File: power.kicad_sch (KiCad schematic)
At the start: 73 parts, among them J1 436500204, J2 ${MANUFACTURER PART NUMBER}, J3 ${MANUFACTURER PART NUMBER}, J4 398800302, J5 398800302, J6 398800302, J7 398800302, U2 INA229AQDGSRQ1, U3 ${MANUFACTURER PART NUMBER}, U4 ${MANUFACTURER PART NUMBER}

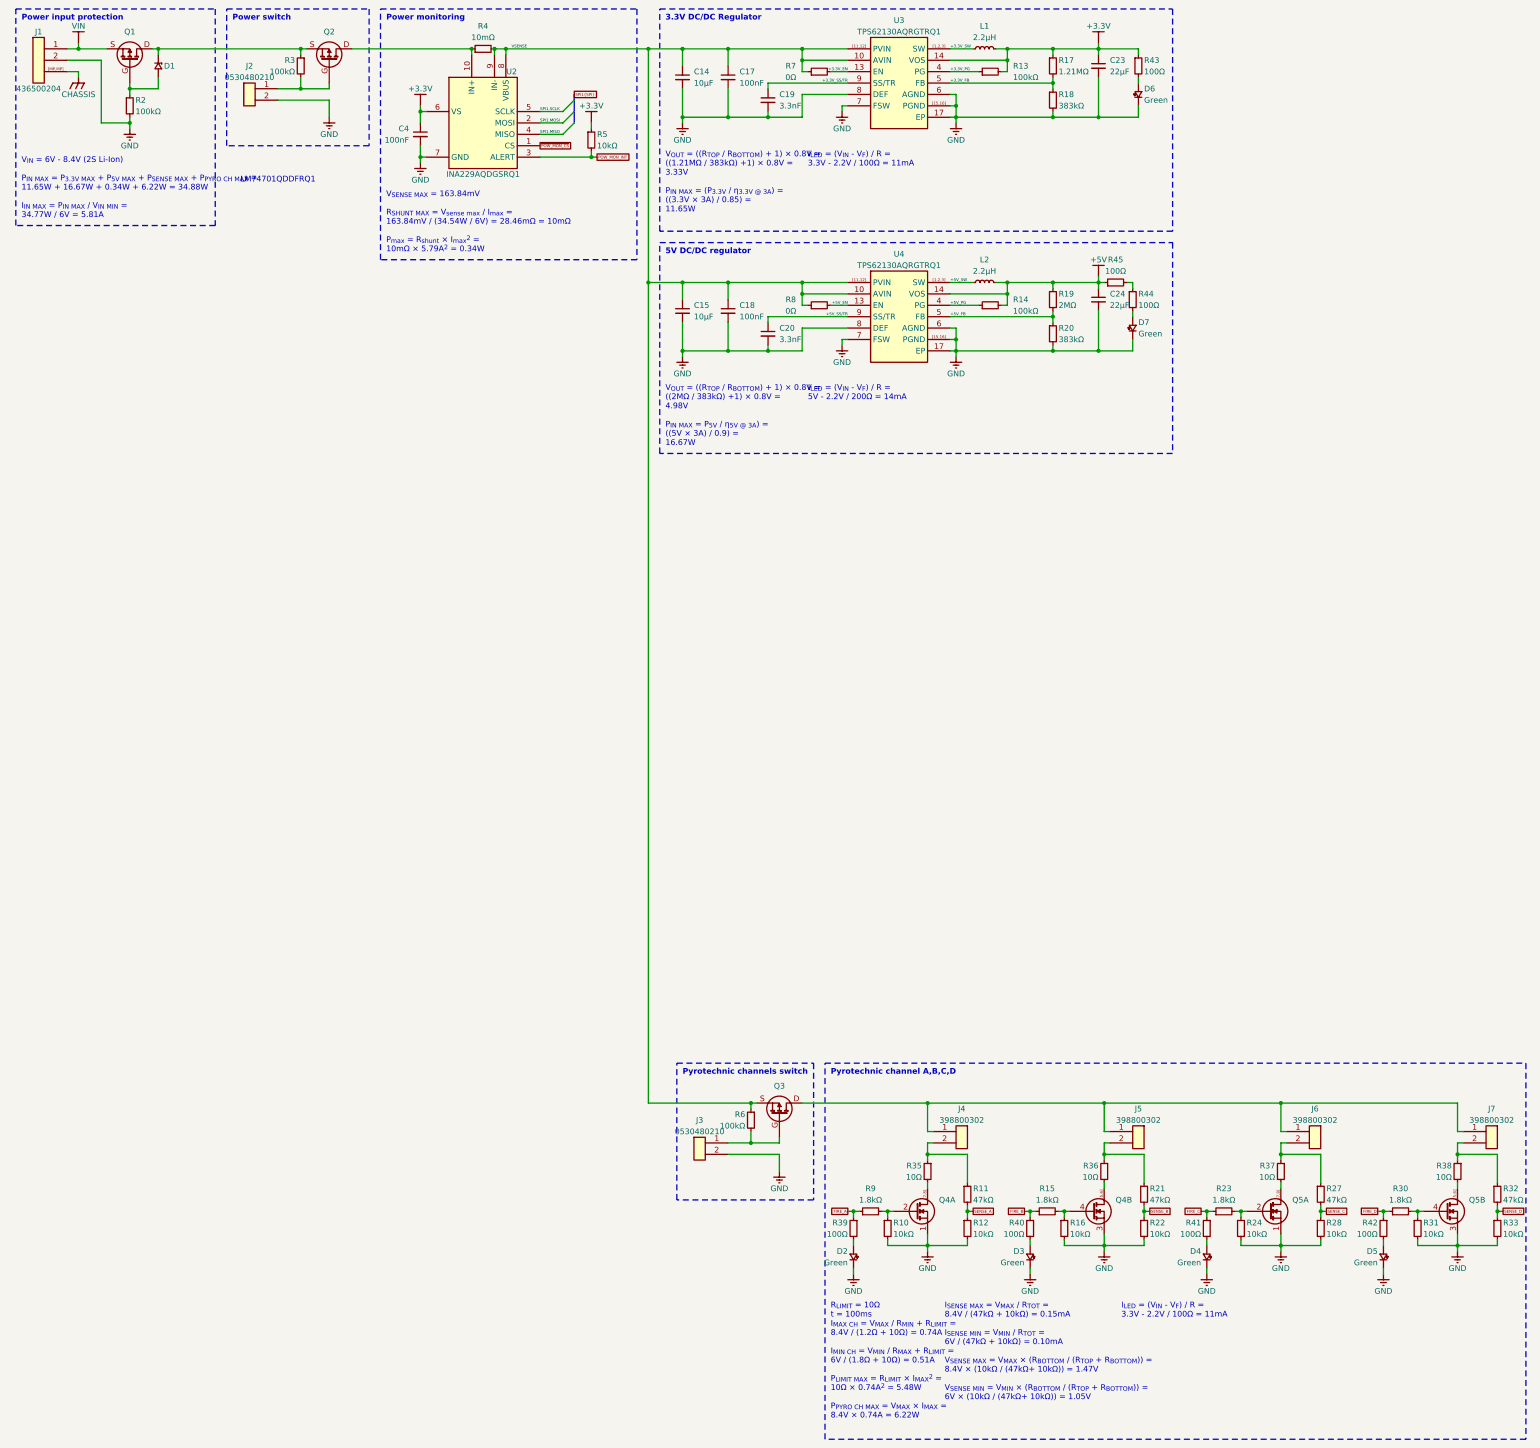
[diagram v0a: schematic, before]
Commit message: Update to power section
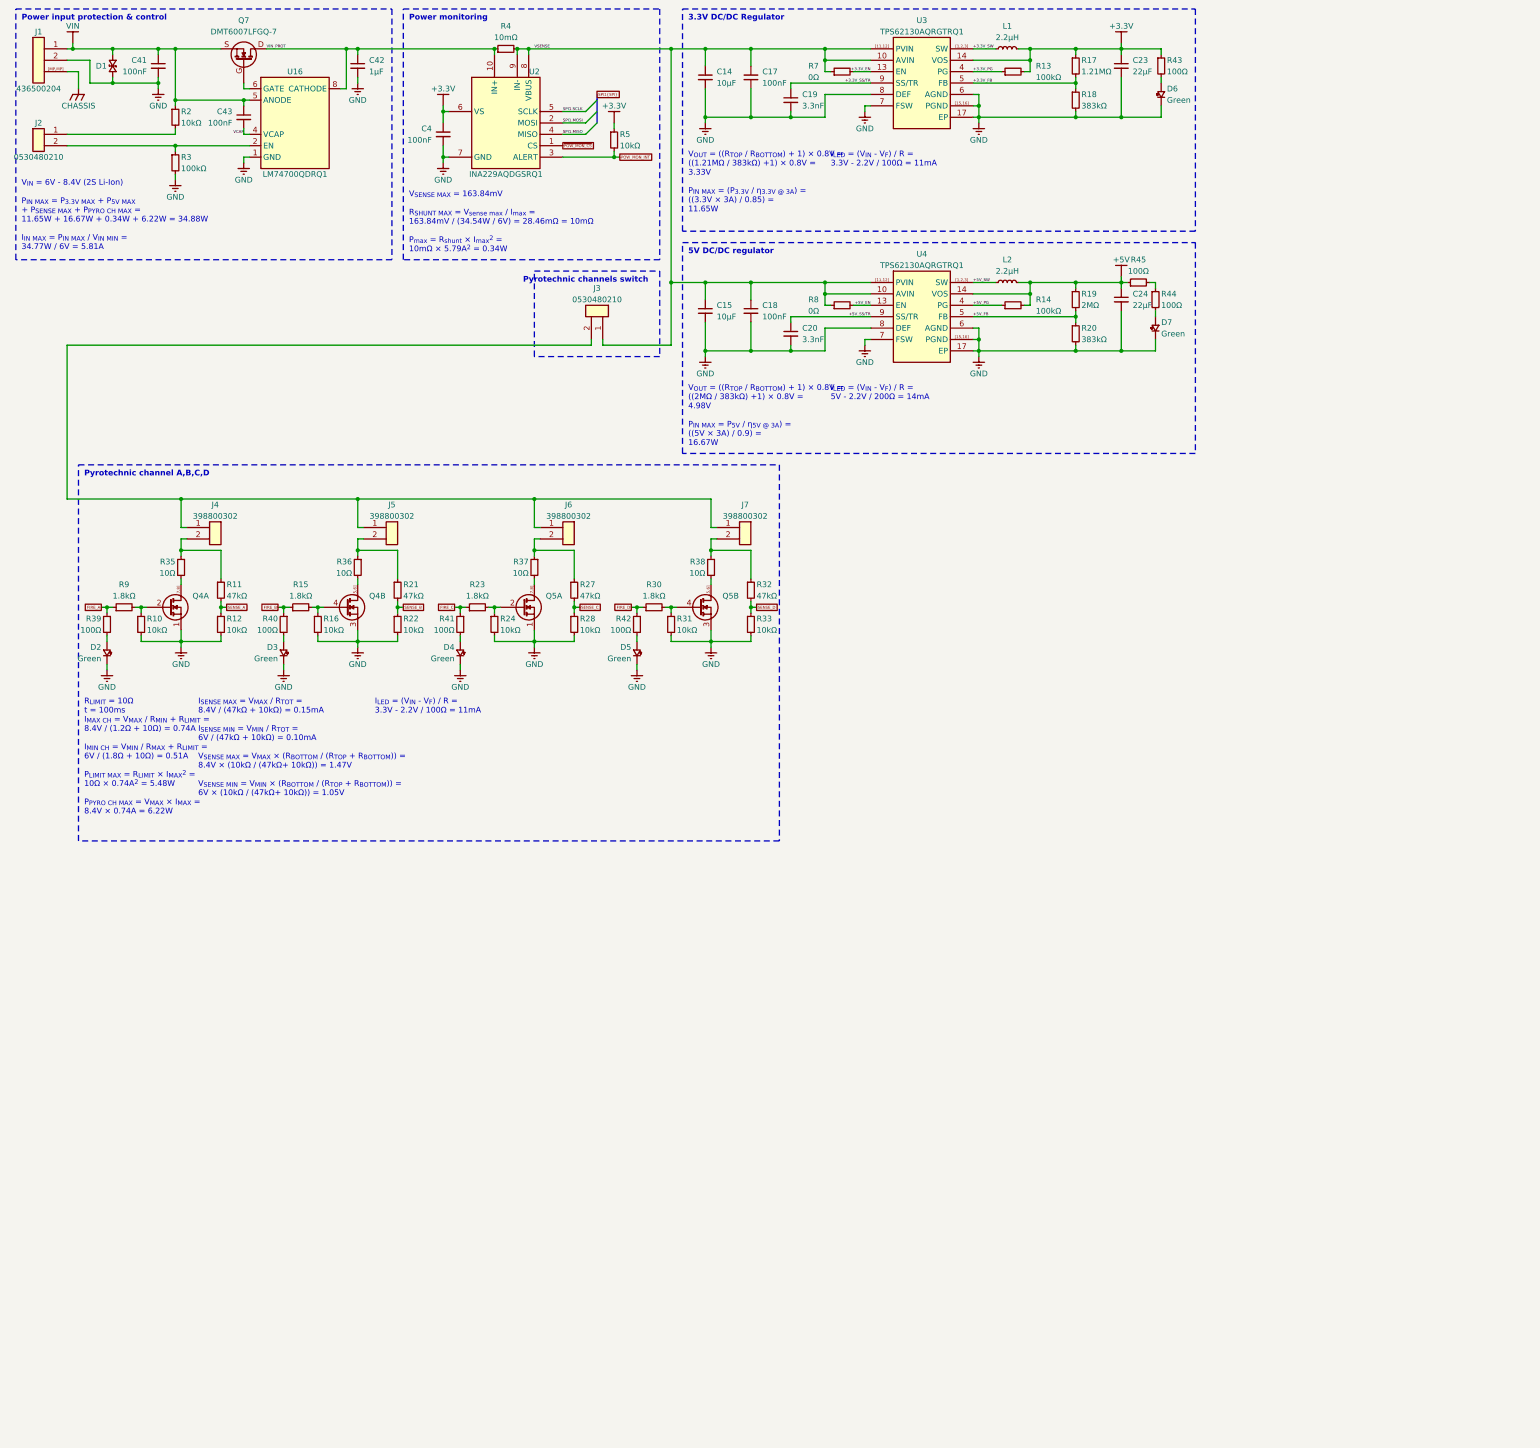
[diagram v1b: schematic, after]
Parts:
- removed D1: (no value), passive_diode:SZSMF20AT1G, symbol passive_diode:SZSMF20AT1G
- removed Q1, Q2, Q3: (no value), passive_mosfet:SQJ211ELP-T1_GE3, symbol passive_mosfet:SQJ211ELP-T1_GE3
- removed R2, R6: ${RESISTANCE}, passive_resistor:R_0603_Density_Nominal, symbol passive_resistor:CRCW0603100KFKEE
- added C41, C43: ${CAPACITANCE}, passive_capacitor:C_0603_Density_Nominal, symbol passive_capacitor:C0603C104J3RACAUTO
- added C42: ${CAPACITANCE}, passive_capacitor:C_0805_Density_Nominal, symbol passive_capacitor:C0805C105J3RECAUTO
- added D1: (no value), passive_diode:SZSMF4L17CAT3G, symbol passive_diode:SZSMF4L17CAT3G
- added Q7: ${MANUFACTURER PART NUMBER}, passive_mosfet:DMT6007LFGQ-7, symbol passive_mosfet:DMT6007LFGQ-7
- added R2: ${RESISTANCE}, passive_resistor:R_0603_Density_Nominal, symbol passive_resistor:CRCW060310K0FKEAHP
- added U16: ${MANUFACTURER PART NUMBER}, ic_power:LM74700QDRQ1, symbol ic_power:LM74700QDRQ1
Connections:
- net GND: now also R3.2, C41.2, C42.2, D1.2, U16.1 (GND); no longer J2.2, J3.2
- net VIN: now also C41.1, C43.1, D1.1, Q7.S, R2.1, U16.5 (ANODE)
- net VSENSE: now also J3.1
- net at R3.1: now also J2.2, U16.2 (EN)
- net at J4.1, J5.1, J6.1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: now also J3.2
- net VIN_PROT: now reaches R4.1, U2.10 (IN+)
- net VIN_PROT: now also C42.1, Q7.D, U16.8 (CATHODE)
- net at J2.1: now also R2.2; no longer R3.2
- new net: Q7.G, U16.6 (GATE)
- new net VCAP: C43.2, U16.4 (VCAP)
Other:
- note added: "Power input protection & control"
- note removed: "LM74701QDDFRQ1"
- note removed: "Power input protection"
- note removed: "Power switch"
- moved on the sheet: C14, C15, C17, C18, C19, C20, C23, C24, C4, D2, D3, D4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
